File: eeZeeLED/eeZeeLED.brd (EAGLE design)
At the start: 11.2 x 6.6 mm, 4 parts

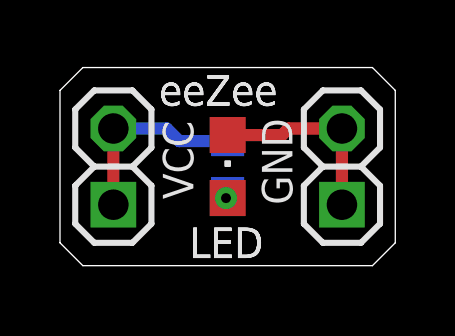
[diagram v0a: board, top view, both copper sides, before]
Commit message: Updated layout, silk, added URL
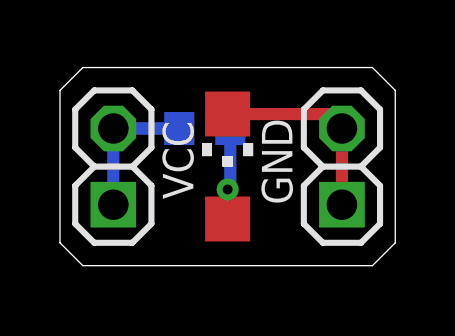
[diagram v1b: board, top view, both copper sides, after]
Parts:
- LED1: device bt_opto:CHIPLED_0805 -> bt_opto:CHIPLED_1206
- moved R1 1.48 mm to (4.83, 4.57), turned to 0 degrees
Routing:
- net N$1: track 0.26 -> 3.06 mm
- net N$3: track 6.52 -> 4.74 mm
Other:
- board text added: "R0.2"
- board text added: "is.gd/EZled"
- board text removed: "R1"
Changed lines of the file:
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@@
 <wire x1="10.414" y1="6.604" x2="0.762" y2="6.604" width="0" layer="20"/>
 <wire x1="0.762" y1="6.604" x2="0" y2="5.842" width="0" layer="20"/>
-<text x="3.302" y="5.334" size="1.016" layer="25" font="vector">eeZee</text>
-<text x="4.318" y="0.254" size="1.016" layer="25" font="vector">LED</text>
+<text x="7.874" y="2.794" size="1.016" layer="26" font="vector" rot="MR0">eeZee</text>
+<text x="7.874" y="1.524" size="1.016" layer="26" font="vector" rot="MR0">LED</text>
+<text x="9.144" y="5.588" size="0.8128" layer="26" font="vector" rot="MR0">is.gd/EZled</text>
+<text x="7.874" y="0.254" size="1.016" layer="26" font="vector" rot="MR0">R0.2</text>
 <wire x1="0.508" y1="1.397" x2="0.508" y2="2.667" width="0.2032" layer="121"/>
 <wire x1="0.508" y1="2.667" x2="1.143" y2="3.302" width="0.2032" layer="121"/>
@@
 <wire x1="10.668" y1="5.207" x2="10.668" y2="3.937" width="0.2032" layer="121"/>
 <wire x1="10.668" y1="3.937" x2="10.033" y2="3.302" width="0.2032" layer="121"/>
-<rectangle x1="5.488" y1="3.302" x2="5.688" y2="3.502" layer="121"/>
-<text x="3.302" y="5.334" size="1.016" layer="121" font="vector" ratio="20">eeZee</text>
-<text x="4.318" y="0.254" size="1.016" layer="121" font="vector" ratio="20">LED</text>
-<text x="6.477" y="2.667" size="1.016" layer="122" font="vector" ratio="20" rot="MR90">R1</text>
+<rectangle x1="4.7379875" y1="3.6520125" x2="5.06300625" y2="4.07700625" layer="121"/>
+<rectangle x1="6.11299375" y1="3.6520125" x2="6.4380125" y2="4.07700625" layer="121"/>
+<rectangle x1="5.41299375" y1="3.302" x2="5.76300625" y2="3.6520125" layer="121"/>
+<text x="7.874" y="2.794" size="1.016" layer="122" font="vector" ratio="20" rot="MR0">eeZee</text>
+<text x="7.874" y="1.524" size="1.016" layer="122" font="vector" ratio="20" rot="MR0">LED</text>
+<text x="9.144" y="5.588" size="0.8128" layer="122" font="vector" ratio="25" rot="MR0">is.gd/EZled</text>
+<text x="7.874" y="0.254" size="1.016" layer="122" font="vector" ratio="20" rot="MR0">R0.2</text>
 <text x="3.429" y="4.826" size="1.016" layer="121" font="vector" ratio="20" rot="R270">VCC</text>
 <text x="7.747" y="2.032" size="1.016" layer="121" font="vector" ratio="20" rot="R90">GND</text>
@@
 </autorouter>
 <elements>
-<element name="LED1" library="bt_opto" package="CHIPLED_0805" value="" x="5.588" y="3.302" smashed="yes">
+<element name="LED1" library="bt_opto" package="CHIPLED_1206" value="" x="5.588" y="3.302" smashed="yes">
 <attribute name="VALUE" x="8.128" y="2.032" size="1.27" layer="27" rot="R90"/>
 </element>
-<element name="R1" library="rcl" package="R0603" value="330" x="5.588" y="3.302" smashed="yes" rot="MR90">
-<attribute name="NAME" x="6.477" y="2.667" size="1.016" layer="26" font="vector" rot="MR90"/>
-</element>
+<element name="R1" library="rcl" package="R0603" value="330" x="4.826" y="4.572" smashed="yes" rot="MR0"/>
 <element name="JP1" library="pinhead-2" package="1X02-S" value="VCC" x="1.778" y="3.302" smashed="yes" rot="R90">
 <attribute name="VALUE" x="3.429" y="4.826" size="1.016" layer="27" font="vector" rot="R270"/>
@@
 <contactref element="LED1" pad="A"/>
 <contactref element="R1" pad="1"/>
-<wire x1="5.588" y1="2.252" x2="5.534" y2="2.252" width="0.4064" layer="1"/>
-<wire x1="5.534" y1="2.252" x2="5.588" y2="2.452" width="0.4064" layer="16"/>
-<via x="5.534" y="2.252" extent="1-16" drill="0.3302"/>
+<wire x1="5.588" y1="1.552" x2="5.588" y2="2.54" width="0.4064" layer="1"/>
+<via x="5.588" y="2.54" extent="1-16" drill="0.3302"/>
+<wire x1="5.676" y1="4.572" x2="5.676" y2="2.628" width="0.4064" layer="16"/>
+<wire x1="5.676" y1="2.628" x2="5.588" y2="2.54" width="0.4064" layer="16"/>
 </signal>
 <signal name="N$2">
@@
 <contactref element="JP2" pad="2"/>
 <wire x1="9.398" y1="4.572" x2="9.398" y2="2.032" width="0.4064" layer="1"/>
-<wire x1="5.588" y1="4.352" x2="7.4" y2="4.352" width="0.4064" layer="1"/>
-<wire x1="7.4" y1="4.352" x2="7.62" y2="4.572" width="0.4064" layer="1"/>
-<wire x1="7.62" y1="4.572" x2="9.398" y2="4.572" width="0.4064" layer="1"/>
+<wire x1="5.588" y1="5.052" x2="8.918" y2="5.052" width="0.4064" layer="1"/>
+<wire x1="8.918" y1="5.052" x2="9.398" y2="4.572" width="0.4064" layer="1"/>
 </signal>
 <signal name="N$3">
@@
 <contactref element="R1" pad="2"/>
 <contactref element="JP1" pad="2"/>
-<wire x1="1.778" y1="2.032" x2="1.778" y2="4.572" width="0.4064" layer="1"/>
-<wire x1="5.588" y1="4.152" x2="3.976" y2="4.152" width="0.4064" layer="16"/>
-<wire x1="3.976" y1="4.152" x2="3.556" y2="4.572" width="0.4064" layer="16"/>
-<wire x1="3.556" y1="4.572" x2="1.778" y2="4.572" width="0.4064" layer="16"/>
+<wire x1="1.778" y1="2.032" x2="1.778" y2="4.572" width="0.4064" layer="16"/>
+<wire x1="3.976" y1="4.572" x2="1.778" y2="4.572" width="0.4064" layer="16"/>
 </signal>
 </signals>
